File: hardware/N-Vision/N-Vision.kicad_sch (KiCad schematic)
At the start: 2 parts, among them J1 547220164, J2 555600168

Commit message: Update footprints (one needed to be reversed)
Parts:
- J1: footprint CONN_54722-0164_MOL -> footprints:CONN_54722-0164_MOL
- J2: footprint CON_555600168 -> footprints:CONN_55560-0168_MOL
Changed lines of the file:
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@@
 			)
 		)
-		(property "Footprint" "CONN_54722-0164_MOL"
+		(property "Footprint" "footprints:CONN_54722-0164_MOL"
 			(at 45.72 31.75 0)
 			(hide yes)
@@
 			)
 		)
-		(property "Footprint" "CON_555600168"
+		(property "Footprint" "footprints:CONN_55560-0168_MOL"
 			(at 71.12 31.75 0)
 			(hide yes)

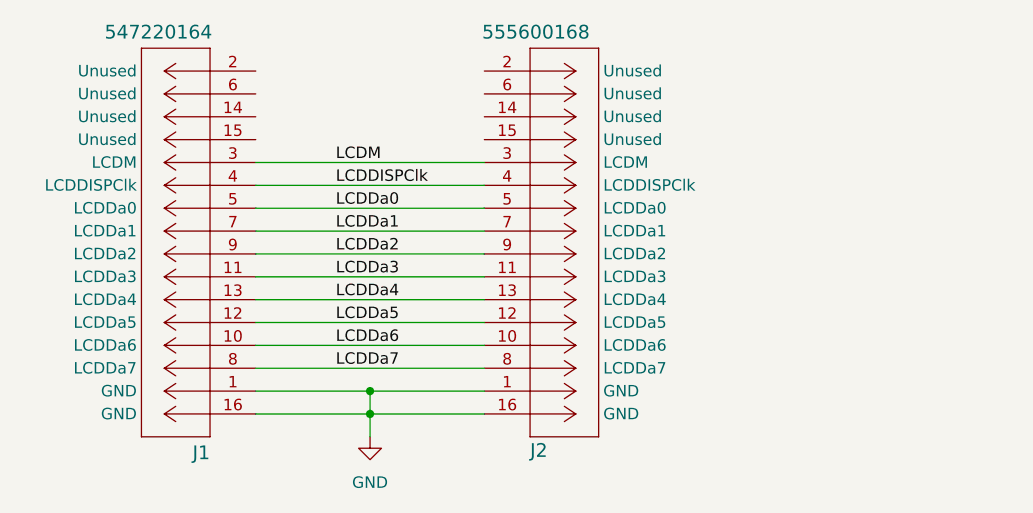
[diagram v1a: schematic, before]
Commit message: Update BOM, add FPC connector.
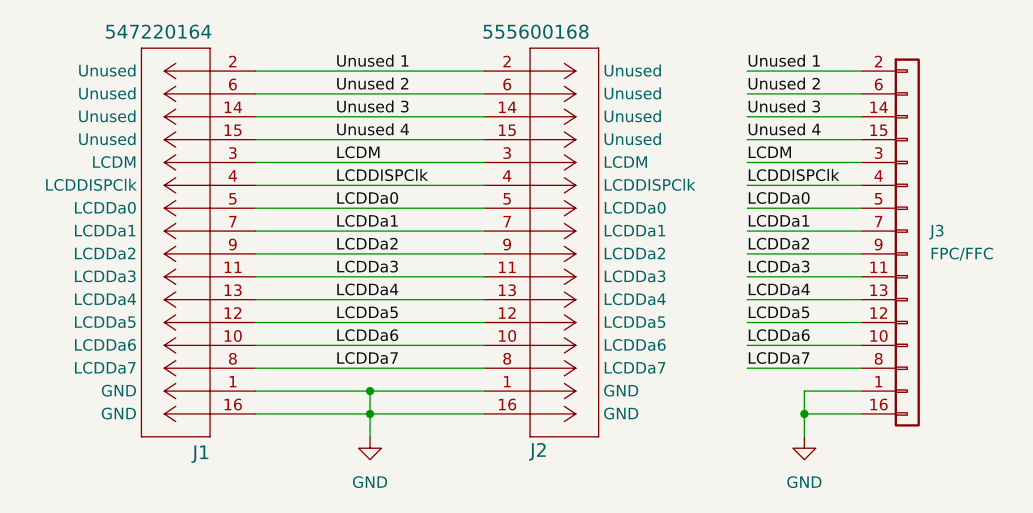
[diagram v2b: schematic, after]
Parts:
- added J3: FPC/FFC, footprints:FPC-16P-0.5mm, symbol Connector_Generic:Conn_01x16
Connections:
- net GND: now also J3.1 (Pin_1), J3.16 (Pin_16)
- net LCDDISPClk: now also J3.4 (Pin_4)
- net LCDDa0: now also J3.5 (Pin_5)
- net LCDDa1: now also J3.7 (Pin_7)
- net LCDDa2: now also J3.9 (Pin_9)
- net LCDDa3: now also J3.11 (Pin_11)
- net LCDDa4: now also J3.13 (Pin_13)
- net LCDDa5: now also J3.12 (Pin_12)
- net LCDDa6: now also J3.10 (Pin_10)
- net LCDDa7: now also J3.8 (Pin_8)
- net LCDM: now also J3.3 (Pin_3)
- net Unused 3: now reaches J1.14 (Unused)
- net Unused 3: now also J2.14 (Unused), J3.14 (Pin_14)
- net Unused 4: now reaches J1.15 (Unused)
- net Unused 4: now also J2.15 (Unused), J3.15 (Pin_15)
- net Unused 1: now reaches J1.2 (Unused)
- net Unused 1: now also J2.2 (Unused), J3.2 (Pin_2)
- net Unused 2: now reaches J1.6 (Unused)
- net Unused 2: now also J2.6 (Unused), J3.6 (Pin_6)
